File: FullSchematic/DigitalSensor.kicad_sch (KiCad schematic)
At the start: 8 parts, among them P1 Touch Pad

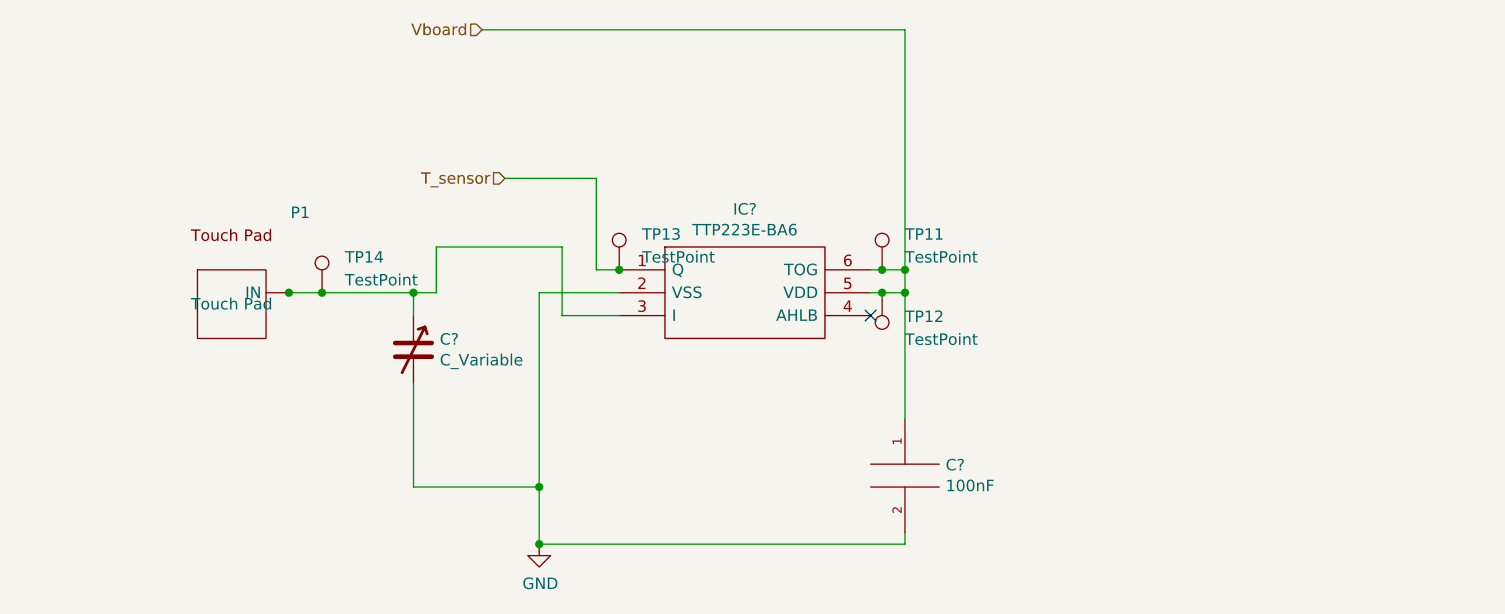
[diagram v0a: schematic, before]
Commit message: Added uvlo circuit
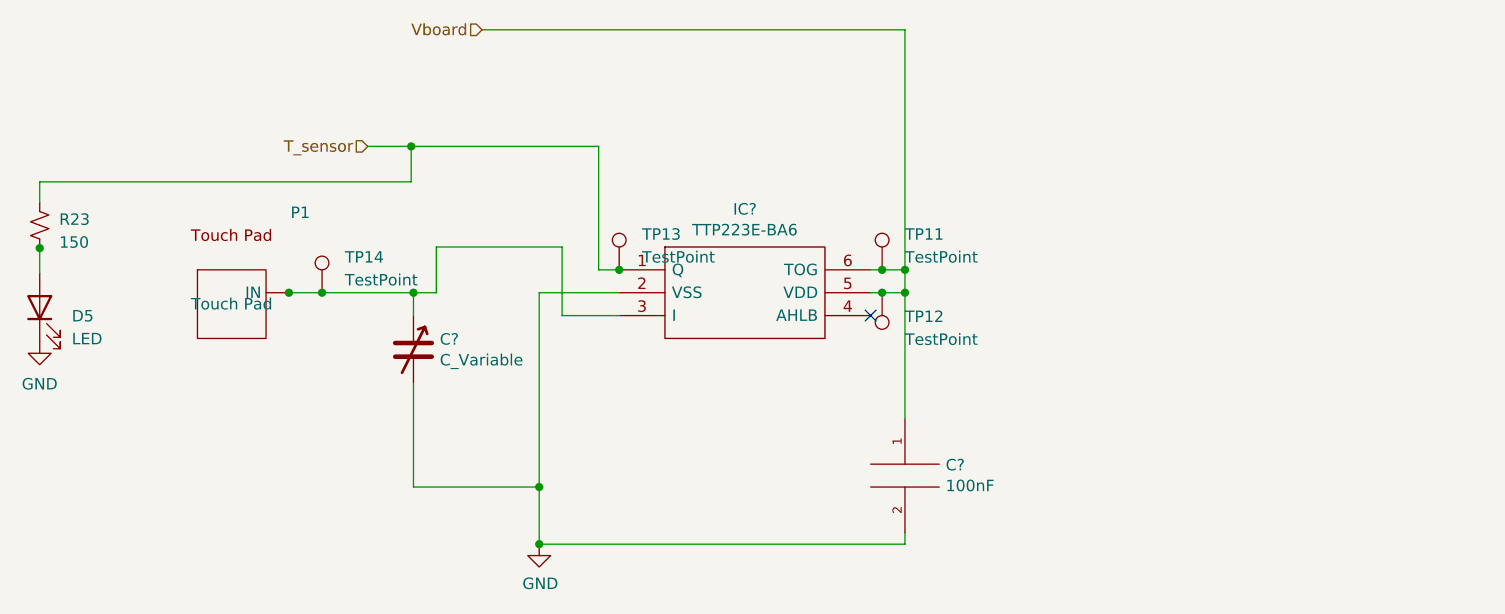
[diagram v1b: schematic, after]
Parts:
- added D5: LED, LED_SMD:LED_0201_0603Metric, symbol Device:LED
- added R23: 150, Resistor_SMD:R_0201_0603Metric, symbol Device:R_Small_US
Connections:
- net GND: now also D5.1 (K)
- net T_sensor: now also R23.1
- new net: D5.2 (A), R23.2
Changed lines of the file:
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@@
   (junction (at 105.41 97.79) (diameter 0) (color 0 0 0 0)
   )
+  (junction (at 74.041 92.837) (diameter 0) (color 0 0 0 0)
+  )
   (junction (at 129.54 119.38) (diameter 0) (color 0 0 0 0)
   )
@@
   )
   (junction (at 101.727 97.79) (diameter 0) (color 0 0 0 0)
+  )
+  (junction (at 115.316 81.534) (diameter 0) (color 0 0 0 0)
   )
   (junction (at 129.54 125.73) (diameter 0) (color 0 0 0 0)
@@
     (stroke (width 0) (type default))
   )
-  (wire (pts (xy 135.89 95.25) (xy 138.43 95.25))
+  (wire (pts (xy 136.144 95.25) (xy 138.43 95.25))
     (stroke (width 0) (type default))
   )
@@
     (stroke (width 0) (type default))
   )
+  (wire (pts (xy 115.316 81.534) (xy 115.316 85.471))
+    (stroke (width 0) (type default))
+  )
+  (wire (pts (xy 74.041 92.837) (xy 74.041 95.631))
+    (stroke (width 0) (type default))
+  )
   (wire (pts (xy 115.57 97.79) (xy 118.11 97.79))
     (stroke (width 0) (type default))
@@
     (stroke (width 0) (type default))
   )
-  (wire (pts (xy 125.73 85.09) (xy 135.89 85.09))
+  (wire (pts (xy 110.49 81.534) (xy 115.316 81.534))
     (stroke (width 0) (type default))
   )
@@
     (stroke (width 0) (type default))
   )
+  (wire (pts (xy 115.316 81.534) (xy 136.144 81.534))
+    (stroke (width 0) (type default))
+  )
   (wire (pts (xy 170.18 111.76) (xy 170.18 97.79))
     (stroke (width 0) (type default))
@@
     (stroke (width 0) (type default))
   )
+  (wire (pts (xy 74.041 92.71) (xy 74.041 92.837))
+    (stroke (width 0) (type default))
+  )
   (wire (pts (xy 129.54 119.38) (xy 129.54 125.73))
     (stroke (width 0) (type default))
@@
     (stroke (width 0) (type default))
   )
-  (wire (pts (xy 135.89 85.09) (xy 135.89 95.25))
+  (wire (pts (xy 136.144 81.534) (xy 136.144 95.25))
     (stroke (width 0) (type default))
   )
@@
     (stroke (width 0) (type default))
   )
+  (wire (pts (xy 74.041 85.471) (xy 74.041 87.757))
+    (stroke (width 0) (type default))
+  )
   (wire (pts (xy 170.18 95.25) (xy 167.64 95.25))
     (stroke (width 0) (type default))
   )
-  (hierarchical_label "T_sensor" (shape input) (at 125.73 85.09 180) (fields_autoplaced)
+  (wire (pts (xy 115.316 85.471) (xy 74.041 85.471))
+    (stroke (width 0) (type default))
+  )
+  (hierarchical_label "T_sensor" (shape input) (at 110.49 81.534 180) (fields_autoplaced)
     (effects (font (size 1.27 1.27)) (justify right))
   )
@@
     )
   )
+  (symbol (lib_id "power:GND") (at 74.041 103.251 0) (unit 1)
+    (in_bom yes) (on_board yes) (dnp no) (fields_autoplaced)
+    (property "Reference" "#PWR019" (at 74.041 109.601 0)
+      (effects (font (size 1.27 1.27)) hide)
+    )
+    (property "Value" "GND" (at 74.041 107.95 0)
+      (effects (font (size 1.27 1.27)))
+    )
+    (property "Footprint" "" (at 74.041 103.251 0)
+      (effects (font (size 1.27 1.27)) hide)
+    )
+    (property "Datasheet" "" (at 74.041 103.251 0)
+      (effects (font (size 1.27 1.27)) hide)
+    )
+    (pin "1")
+    (instances
+      (project "FullSchematic"
+        (path "/5dd86611-a33d-45ee-946c-01c599f30b12/ef09fc32-79b3-4972-8ce2-fc52eddbfbb8/00000000-0000-0000-0000-0000640c1ec4"
+          (reference "#PWR019") (unit 1)
+        )
+      )
+    )
+  )
   (symbol (lib_id "Connector:TestPoint") (at 105.41 97.79 0) (unit 1)
     (in_bom yes) (on_board yes) (dnp no) (fields_autoplaced)
@@
         )
       )
+    )
+  )
+  (symbol (lib_id "Device:R_Small_US") (at 74.041 90.297 0) (unit 1)
+    (in_bom yes) (on_board yes) (dnp no) (fields_autoplaced)
+    (property "Reference" "R23" (at 76.2 89.662 0)
+      (effects (font (size 1.27 1.27)) (justify left))
+    )
+    (property "Value" "150" (at 76.2 92.202 0)
+      (effects (font (size 1.27 1.27)) (justify left))
+    )
+    (property "Footprint" "Resistor_SMD:R_0201_0603Metric" (at 74.041 90.297 0)
+      (effects (font (size 1.27 1.27)) hide)
+    )
+    (property "Datasheet" "~" (at 74.041 90.297 0)
+      (effects (font (size 1.27 1.27)) hide)
+    )
+    (pin "1")
+    (pin "2")
+    (instances
+      (project "FullSchematic"
+        (path "/5dd86611-a33d-45ee-946c-01c599f30b12/ef09fc32-79b3-4972-8ce2-fc52eddbfbb8/00000000-0000-0000-0000-0000640c1ec4"
+          (reference "R23") (unit 1)
+        )
+      )
+    )
+  )
+  (symbol (lib_id "Device:LED") (at 74.041 99.441 90) (unit 1)
+    (in_bom yes) (on_board yes) (dnp no) (fields_autoplaced)
+    (property "Reference" "D5" (at 77.597 100.3935 90)
+      (effects (font (size 1.27 1.27)) (justify right))
+    )
+    (property "Value" "LED" (at 77.597 102.9335 90)
+      (effects (font (size 1.27 1.27)) (justify right))
+    )
+    (property "Footprint" "LED_SMD:LED_0201_0603Metric" (at 74.041 99.441 0)
+      (effects (font (size 1.27 1.27)) hide)
+    )
+    (property "Datasheet" "~" (at 74.041 99.441 0)
+      (effects (font (size 1.27 1.27)) hide)
+    )
+    (pin "1")
+    (pin "2")
+    (instances
+      (project "FullSchematic"
+        (path "/5dd86611-a33d-45ee-946c-01c599f30b12/ef09fc32-79b3-4972-8ce2-fc52eddbfbb8/00000000-0000-0000-0000-0000640c1ec4"
+          (reference "D5") (unit 1)
+        )
+      )

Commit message: Confirmed part numbers and prices
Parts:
- removed C?: C_Variable, Capacitor_SMD:C_Trimmer_Murata_TZC3, symbol Device:C_Variable
- added C5: 20pF, Capacitor_THT:C_Disc_D4.7mm_W2.5mm_P5.00mm, symbol Device:C
- C?: footprint Capacitor_THT:CP_Axial_L10.0mm_D4.5mm_P15.00mm_Horizontal -> Capacitor_THT:C_Disc_D4.3mm_W1.9mm_P5.00mm; JLCPCB Part # C24497 -> C409812; Populate (none) -> Yes
- D5: JLCPCB Part # (none) -> C165982; Populate (none) -> Yes; Price (none) -> 0.0212; Price ( 1 board) (none) -> 0.0212; Price (5 boards) (none) -> 0.106
- IC?: Populate (none) -> Yes
- R23: value 150 -> 150R; JLCPCB Part # (none) -> C136932; Populate (none) -> Yes; Price (none) -> 0.01; Price ( 1 board) (none) -> 0.01; Price (5 boards) (none) -> 0.05
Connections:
- net GND: now also C5.2
- net at IC?.3 (I), P1. (IN), TP14.1: now also C5.1
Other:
- note added: "Pin 6 (TOG) pulled high to cause toggle mode"
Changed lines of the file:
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@@
     (stroke (width 0) (type default))
+  )
+  (text "Pin 6 (TOG) pulled high to cause toggle mode\n" (at 180.467 95.631 0)
+    (effects (font (size 1.27 1.27)) (justify left bottom))
   )
   (hierarchical_label "T_sensor" (shape input) (at 110.49 81.534 180) (fields_autoplaced)
@@
     )
     (property "Price (5 boards)" "0.5" (at 138.43 95.25 0)
+      (effects (font (size 1.27 1.27)) hide)
+    )
+    (property "Populate" "Yes" (at 138.43 95.25 0)
       (effects (font (size 1.27 1.27)) hide)
     )
@@
       (effects (font (size 1.27 1.27)) (justify left))
     )
-    (property "Footprint" "Capacitor_THT:CP_Axial_L10.0mm_D4.5mm_P15.00mm_Horizontal" (at 170.18 118.11 0)
+    (property "Footprint" "Capacitor_THT:C_Disc_D4.3mm_W1.9mm_P5.00mm" (at 170.18 118.11 0)
       (effects (font (size 1.27 1.27)) hide)
     )
@@
       (effects (font (size 1.27 1.27)) hide)
     )
-    (property "JLCPCB Part #" "C24497" (at 170.18 118.11 0)
+    (property "JLCPCB Part #" "C409812" (at 170.18 118.11 0)
+      (effects (font (size 1.27 1.27)) hide)
+    )
+    (property "Populate" "Yes" (at 170.18 118.11 0)
       (effects (font (size 1.27 1.27)) hide)
     )
@@
     )
   )
-  (symbol (lib_id "Device:C_Variable") (at 115.57 104.14 0) (unit 1)
-    (in_bom yes) (on_board yes) (dnp no)
-    (property "Reference" "C?" (at 118.491 102.9716 0)
-      (effects (font (size 1.27 1.27)) (justify left))
-    )
-    (property "Value" "C_Variable" (at 118.491 105.283 0)
-      (effects (font (size 1.27 1.27)) (justify left))
-    )
-    (property "Footprint" "Capacitor_SMD:C_Trimmer_Murata_TZC3" (at 115.57 104.14 0)
+  (symbol (lib_id "Device:C") (at 115.57 104.14 0) (unit 1)
+    (in_bom yes) (on_board yes) (dnp no) (fields_autoplaced)
+    (property "Reference" "C5" (at 119.38 103.505 0)
+      (effects (font (size 1.27 1.27)) (justify left))
+    )
+    (property "Value" "20pF" (at 119.38 106.045 0)
+      (effects (font (size 1.27 1.27)) (justify left))
+    )
+    (property "Footprint" "Capacitor_THT:C_Disc_D4.7mm_W2.5mm_P5.00mm" (at 116.5352 107.95 0)
       (effects (font (size 1.27 1.27)) hide)
     )
@@
       (effects (font (size 1.27 1.27)) hide)
     )
-    (property "Price" "0.3067" (at 115.57 104.14 0)
-      (effects (font (size 1.27 1.27)) hide)
-    )
-    (property "Price ( 1 board)" "0.3067" (at 115.57 104.14 0)
-      (effects (font (size 1.27 1.27)) hide)
-    )
-    (property "Price (5 boards)" "1.54" (at 115.57 104.14 0)
-      (effects (font (size 1.27 1.27)) hide)
-    )
-    (property "JLCPCB Part #" "C125363" (at 115.57 104.14 0)
+    (property "JLCPCB Part #" "C123152" (at 115.57 104.14 0)
+      (effects (font (size 1.27 1.27)) hide)
+    )
+    (property "Price" "0.08" (at 115.57 104.14 0)
+      (effects (font (size 1.27 1.27)) hide)
+    )
+    (property "Price ( 1 board)" "0.08" (at 115.57 104.14 0)
+      (effects (font (size 1.27 1.27)) hide)
+    )
+    (property "Populate" "Yes" (at 115.57 104.14 0)
+      (effects (font (size 1.27 1.27)) hide)
+    )
+    (property "Price (5 boards)" "0.4" (at 115.57 104.14 0)
       (effects (font (size 1.27 1.27)) hide)
     )
@@
     (pin "2")
     (instances
-      (project "Sensors"
-        (path "/0f49447b-394e-4f6a-ab05-2cec98d3964f/00000000-0000-0000-0000-0000640c1ec4"
-          (reference "C?") (unit 1)
-        )
-      )
-      (project "FullSchematic"
-        (path "/5dd86611-a33d-45ee-946c-01c599f30b12/ef09fc32-79b3-4972-8ce2-fc52eddbfbb8/00000000-0000-0000-0000-0000640c1ec4"
-          (reference "C12") (unit 1)
+      (project "FullSchematic"
+        (path "/5dd86611-a33d-45ee-946c-01c599f30b12/ef09fc32-79b3-4972-8ce2-fc52eddbfbb8/00000000-0000-0000-0000-0000640c1ec4"
+          (reference "C5") (unit 1)
         )
       )
@@
       (effects (font (size 1.27 1.27)) (justify left))
     )
-    (property "Value" "150" (at 76.2 92.202 0)
+    (property "Value" "150R" (at 76.2 92.202 0)
       (effects (font (size 1.27 1.27)) (justify left))
     )
@@
     )
     (property "Datasheet" "~" (at 74.041 90.297 0)
+      (effects (font (size 1.27 1.27)) hide)
+    )
+    (property "JLCPCB Part #" "C136932" (at 74.041 90.297 0)
+      (effects (font (size 1.27 1.27)) hide)
+    )
+    (property "Populate" "Yes" (at 74.041 90.297 0)
+      (effects (font (size 1.27 1.27)) hide)
+    )
+    (property "Price" "0.01" (at 74.041 90.297 0)
+      (effects (font (size 1.27 1.27)) hide)
+    )
+    (property "Price ( 1 board)" "0.01" (at 74.041 90.297 0)
+      (effects (font (size 1.27 1.27)) hide)
+    )
+    (property "Price (5 boards)" "0.05" (at 74.041 90.297 0)
       (effects (font (size 1.27 1.27)) hide)
     )
@@
       (effects (font (size 1.27 1.27)) hide)
     )
+    (property "JLCPCB Part #" "C165982" (at 74.041 99.441 0)
+      (effects (font (size 1.27 1.27)) hide)
+    )
+    (property "Price" "0.0212" (at 74.041 99.441 0)
+      (effects (font (size 1.27 1.27)) hide)
+    )
+    (property "Price ( 1 board)" "0.0212" (at 74.041 99.441 0)
+      (effects (font (size 1.27 1.27)) hide)
+    )
+    (property "Price (5 boards)" "0.106" (at 74.041 99.441 0)
+      (effects (font (size 1.27 1.27)) hide)
+    )
+    (property "Populate" "Yes" (at 74.041 99.441 0)
+      (effects (font (size 1.27 1.27)) hide)
+    )

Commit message: generated files
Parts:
- P1, TP11, TP12, TP13, TP14: JLCPCB Part # N/A -> (none)
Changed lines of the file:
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@@
       (effects (font (size 1.27 1.27)) hide)
     )
-    (property "JLCPCB Part #" "N/A" (at 105.41 97.79 0)
+    (property "JLCPCB Part #" "" (at 105.41 97.79 0)
       (effects (font (size 1.27 1.27)) hide)
     )
@@
       (effects (font (size 1.27 1.27)) hide)
     )
-    (property "JLCPCB Part #" "N/A" (at 167.64 97.79 0)
+    (property "JLCPCB Part #" "" (at 167.64 97.79 0)
       (effects (font (size 1.27 1.27)) hide)
     )
@@
       (effects (font (size 1.27 1.27)) hide)
     )
-    (property "JLCPCB Part #" "N/A" (at 138.43 95.25 0)
+    (property "JLCPCB Part #" "" (at 138.43 95.25 0)
       (effects (font (size 1.27 1.27)) hide)
     )
@@
       (effects (font (size 1.27 1.27)) hide)
     )
-    (property "JLCPCB Part #" "N/A" (at 167.64 95.25 0)
+    (property "JLCPCB Part #" "" (at 167.64 95.25 0)
       (effects (font (size 1.27 1.27)) hide)
     )
@@
       (effects (font (size 1.27 1.27)) hide)
     )
-    (property "JLCPCB Part #" "N/A" (at 95.377 99.06 0)
-      (effects (font (size 1.27 1.27)) hide)
-    )
+    (property "JLCPCB Part #" "" (at 95.377 99.06 0)
+      (effects (font (size 1.27 1.27)) hide)
+    )

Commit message: Decreased Price
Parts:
- C?: footprint Capacitor_THT:C_Disc_D4.3mm_W1.9mm_P5.00mm -> Capacitor_SMD:C_1206_3216Metric; JLCPCB Part # C409812 -> C24497
- D5: footprint LED_SMD:LED_0201_0603Metric -> LED_SMD:LED_0805_2012Metric; JLCPCB Part # C165982 -> C2296
- R23: JLCPCB Part # C136932 -> C22808
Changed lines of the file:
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@@
       (effects (font (size 1.27 1.27)) (justify left))
     )
-    (property "Footprint" "Capacitor_THT:C_Disc_D4.3mm_W1.9mm_P5.00mm" (at 170.18 118.11 0)
+    (property "Footprint" "Capacitor_SMD:C_1206_3216Metric" (at 170.18 118.11 0)
       (effects (font (size 1.27 1.27)) hide)
     )
@@
       (effects (font (size 1.27 1.27)) hide)
     )
-    (property "JLCPCB Part #" "C409812" (at 170.18 118.11 0)
+    (property "JLCPCB Part #" "C24497" (at 170.18 118.11 0)
       (effects (font (size 1.27 1.27)) hide)
     )
@@
       (effects (font (size 1.27 1.27)) hide)
     )
-    (property "JLCPCB Part #" "C136932" (at 74.041 90.297 0)
+    (property "JLCPCB Part #" "C22808" (at 74.041 90.297 0)
       (effects (font (size 1.27 1.27)) hide)
     )
@@
       (effects (font (size 1.27 1.27)) (justify right))
     )
-    (property "Footprint" "LED_SMD:LED_0201_0603Metric" (at 74.041 99.441 0)
+    (property "Footprint" "LED_SMD:LED_0805_2012Metric" (at 74.041 99.441 0)
       (effects (font (size 1.27 1.27)) hide)
     )
@@
       (effects (font (size 1.27 1.27)) hide)
     )
-    (property "JLCPCB Part #" "C165982" (at 74.041 99.441 0)
-      (effects (font (size 1.27 1.27)) hide)
-    )
+    (property "JLCPCB Part #" "C2296" (at 74.041 99.441 0)
+      (effects (font (size 1.27 1.27)) hide)
+    )

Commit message: Uploaded final board design
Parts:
- C5: footprint Capacitor_THT:C_Disc_D4.7mm_W2.5mm_P5.00mm -> Capacitor_SMD:C_0805_2012Metric; JLCPCB Part # C123152 -> C1798
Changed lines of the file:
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@@
   (junction (at 170.18 97.79) (diameter 0) (color 0 0 0 0)
   )
+  (junction (at 105.41 97.79) (diameter 0) (color 0 0 0 0)
+  )
   (junction (at 167.64 97.79) (diameter 0) (color 0 0 0 0)
   )
   (junction (at 115.57 97.79) (diameter 0) (color 0 0 0 0)
   )
-  (junction (at 105.41 97.79) (diameter 0) (color 0 0 0 0)
-  )
   (junction (at 74.041 92.837) (diameter 0) (color 0 0 0 0)
   )
@@
   )
   (junction (at 170.18 95.25) (diameter 0) (color 0 0 0 0)
-  )
-  (junction (at 101.727 97.79) (diameter 0) (color 0 0 0 0)
   )
   (junction (at 115.316 81.534) (diameter 0) (color 0 0 0 0)
@@
     (stroke (width 0) (type default))
   )
+  (wire (pts (xy 101.727 97.79) (xy 105.41 97.79))
+    (stroke (width 0) (type default))
+  )
   (wire (pts (xy 74.041 92.837) (xy 74.041 95.631))
     (stroke (width 0) (type default))
@@
     (stroke (width 0) (type default))
   )
-  (wire (pts (xy 101.6 97.79) (xy 101.727 97.79))
-    (stroke (width 0) (type default))
-  )
   (wire (pts (xy 170.18 68.58) (xy 170.18 95.25))
     (stroke (width 0) (type default))
@@
   )
   (wire (pts (xy 166.37 97.79) (xy 167.64 97.79))
-    (stroke (width 0) (type default))
-  )
-  (wire (pts (xy 101.727 97.79) (xy 105.41 97.79))
     (stroke (width 0) (type default))
   )
@@
       (effects (font (size 1.27 1.27)) (justify left))
     )
-    (property "Footprint" "Capacitor_THT:C_Disc_D4.7mm_W2.5mm_P5.00mm" (at 116.5352 107.95 0)
+    (property "Footprint" "Capacitor_SMD:C_0805_2012Metric" (at 116.5352 107.95 0)
       (effects (font (size 1.27 1.27)) hide)
     )
@@
       (effects (font (size 1.27 1.27)) hide)
     )
-    (property "JLCPCB Part #" "C123152" (at 115.57 104.14 0)
-      (effects (font (size 1.27 1.27)) hide)
-    )
+    (property "JLCPCB Part #" "C1798" (at 115.57 104.14 0)
+      (effects (font (size 1.27 1.27)) hide)
+    )
